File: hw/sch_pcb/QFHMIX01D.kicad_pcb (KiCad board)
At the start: 2 copper layers, 90.9 x 90.9 mm, 205 parts, among them J1 HEADER_1x08, J2 +9V, M1 HOLE, M2 HOLE, M3 HOLE, M4 HOLE, M5 HOLE, M6 HOLE, M7 HOLE, M8 HOLE, U1 NCP1117ST33, U11 TPS563249, U12 Si53322, U2 AD8343, U3 AD8343, U5 LT6604-10, U6 MPGA-105+, U7 MPGA-105+, U8 MGVA-63+, U9 MGVA-63+

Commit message: Zmena pouzdra L 0805
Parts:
- L1, L10, L11, L12, L13, L14, L15, L16, L17, L18, L19, L2, L20, L21, L22, L23, L24, L25, L26, L27, L28, L29, L3, L30, L31, L32, L33, L34, L35, L36, L37, L38, L39, L4, L40, L41, L42, L43, L44, L45, L46, L47, L5, L52, L53, L54, L55, L56, L57, L58, L59, L6, L60, L61, L62, L63, L64, L65, L66, L67, L68, L69, L7, L70, L8, L9: footprint Inductor_SMD:L_0805_2012Metric -> Inductor_SMD:L_0805_2012Metric_Pad1.15x1.40mm_HandSolder
- L48: footprint Mlab_L:SMD-0805 -> Inductor_SMD:L_0805_2012Metric_Pad1.15x1.40mm_HandSolder
- L51: footprint Mlab_R:SMD-0805 -> Inductor_SMD:L_0805_2012Metric_Pad1.15x1.40mm_HandSolder

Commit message: Add thermistor #22, align text labels
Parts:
- added D2: BZV55C-3,6V, Diode_SMD:D_MiniMELF, B.Cu at (171.9, 117.3)
- added R16: 24k, Resistor_SMD:R_0805_2012Metric, B.Cu at (167.5, 117.5)
- added TH1: Thermistor, NCP21XV103J03RA, Resistor_SMD:R_0805_2012Metric, B.Cu at (140.5, 98.4)
- moved R3 1.81 mm to (146.8, 97.2)
- moved R6 0.99 mm to (145.4, 91.3), turned to 45 degrees
- moved C12 0.40 mm to (137.6, 87.7)
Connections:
- U11 pad 5: VCC -> /Power/PWR_EN
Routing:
- net /Power/PWR_EN: track 0.00 -> 55.5 mm, vias 0 -> 6
- net VCC: track 69.9 -> 65.6 mm, vias 5 -> 4
- net +5V: track 186.3 -> 182.1 mm
- net Net-(L3-Pad1): track 1.83 -> 2.49 mm
- net GND: vias 510 -> 511
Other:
- board text added: "mlab.cz 2022"
- board text removed: "mlab.cz 2021"

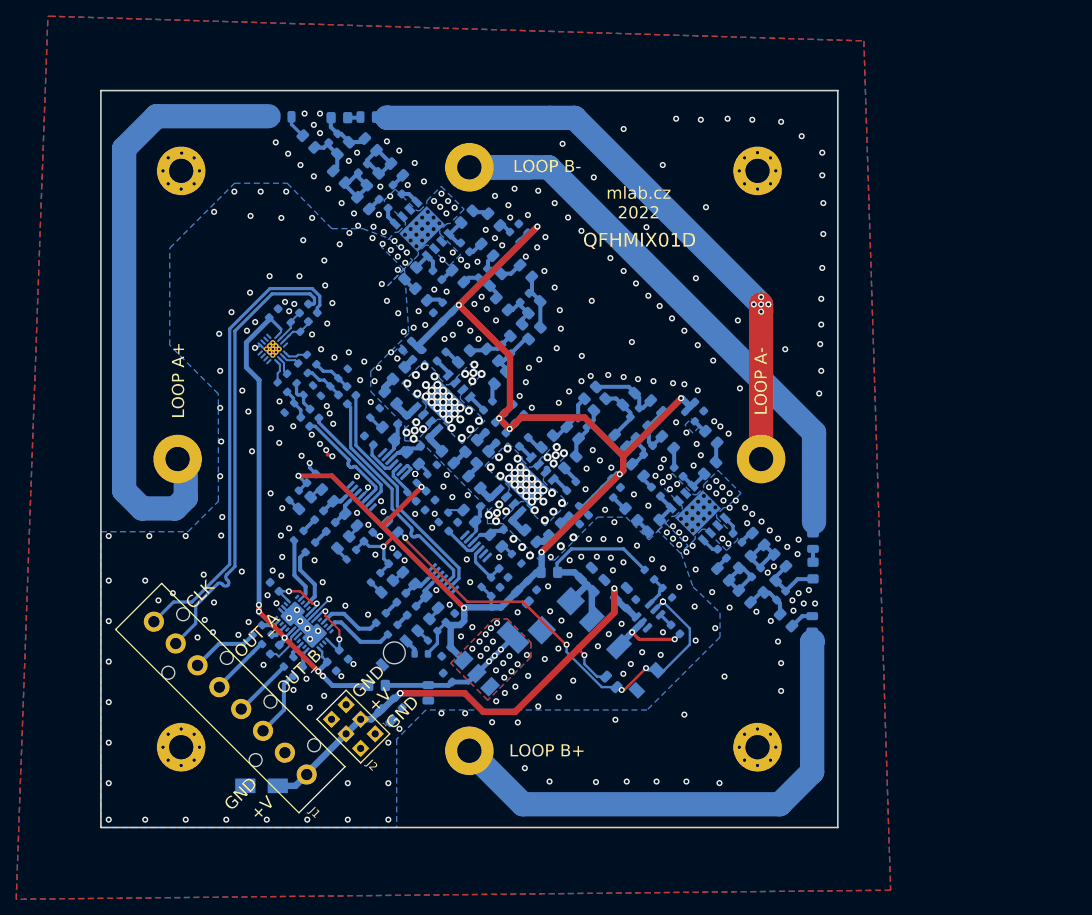
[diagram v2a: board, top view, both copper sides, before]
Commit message: reseni nekterych DRC prolemu
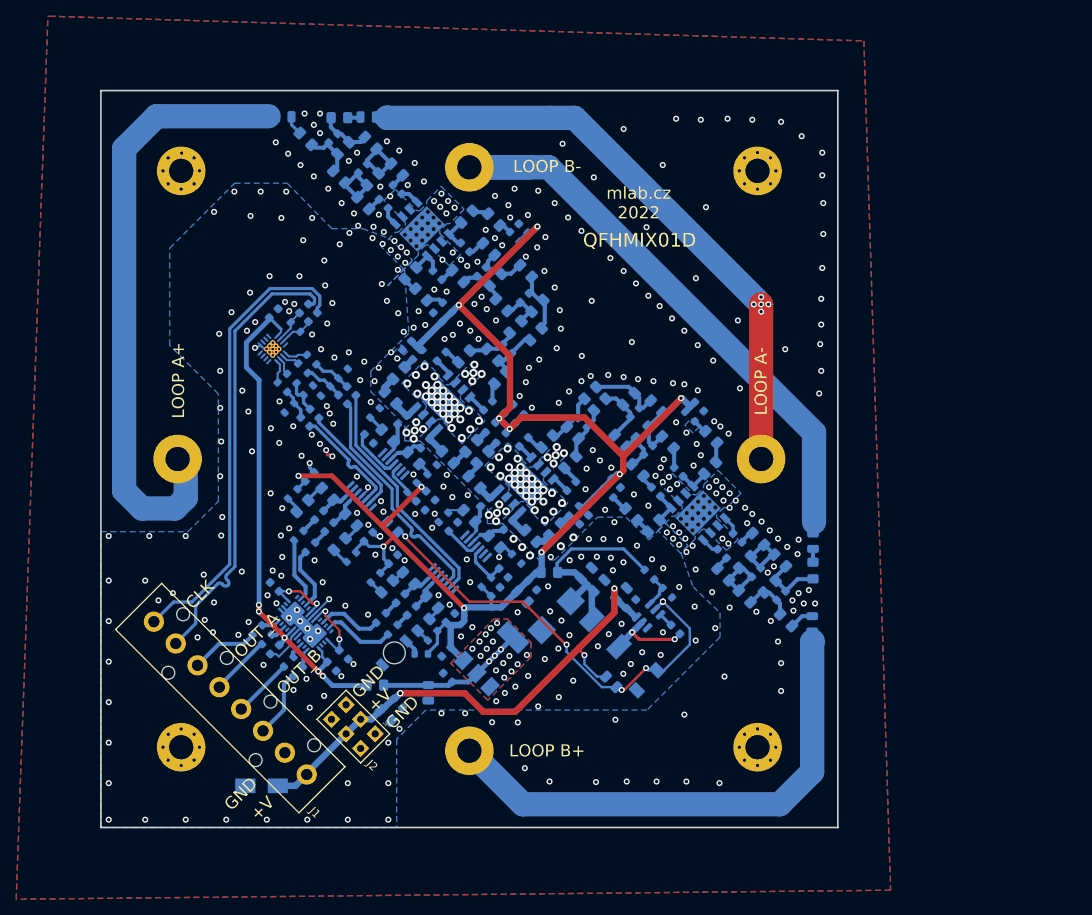
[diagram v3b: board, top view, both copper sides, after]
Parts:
- moved L5 0.50 mm to (129.8, 50.5)
- moved L12 0.49 mm to (134.0, 100.5)
- moved L8 0.47 mm to (129.4, 95.8)
- moved L36 0.42 mm to (158.4, 71.1)
- moved L39 0.40 mm to (155.7, 73.7)
- moved L2 0.31 mm to (139.9, 87.1)
- moved R26 0.30 mm to (135.4, 102.1)
- moved C17 0.27 mm to (130.3, 92.2)
- moved C58 0.26 mm to (151.5, 66.9)
- moved R24 0.25 mm to (128.2, 94.3)
- moved L1 0.22 mm to (153.1, 100.2)
- moved L59 0.22 mm to (152.4, 64.1)
- moved C36 0.22 mm to (144.5, 88.1)
- moved L48 0.21 mm to (138.4, 117.9)
- moved L65 0.21 mm to (158.2, 74.6)
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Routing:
- net GND: track 27.7 -> 24.4 mm, vias 511 -> 510
- net Net-(C12-Pad1): track 4.88 -> 6.51 mm
- net +5V: track 182.1 -> 181.0 mm
- net Net-(C74-Pad2): track 26.4 -> 25.7 mm
- net Net-(C58-Pad2): track 5.60 -> 4.95 mm
- net Net-(C64-Pad2): track 6.83 -> 6.25 mm
- net Net-(C63-Pad2): track 5.27 -> 4.69 mm

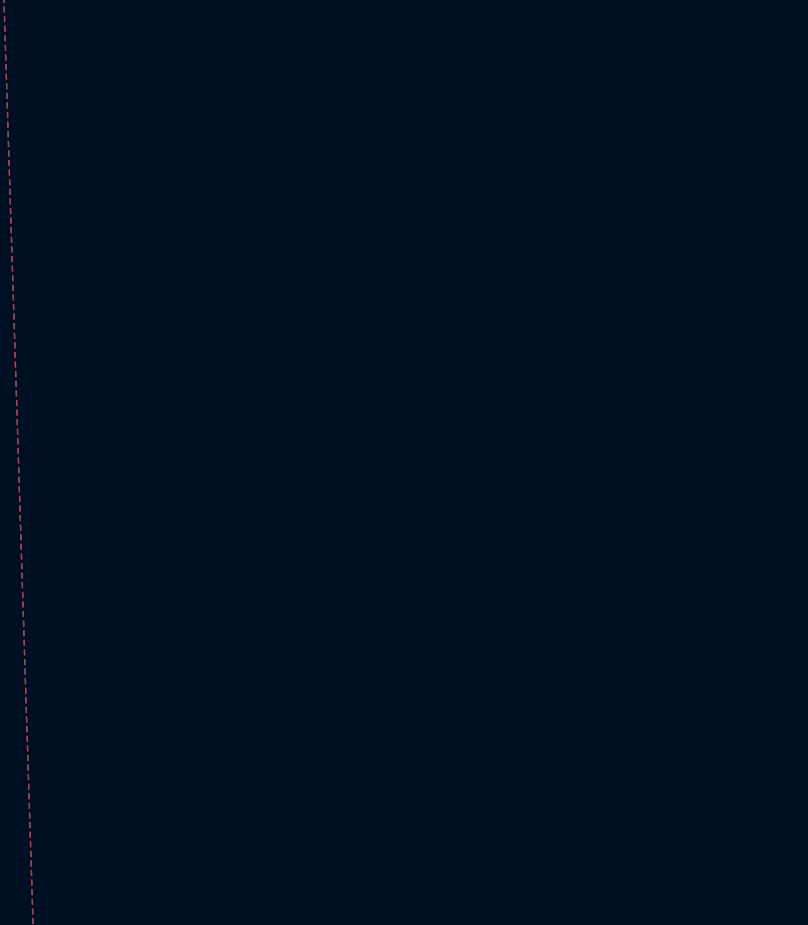
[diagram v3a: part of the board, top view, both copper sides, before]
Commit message: rozpracovani #11 (menic na 5 a 3v3)
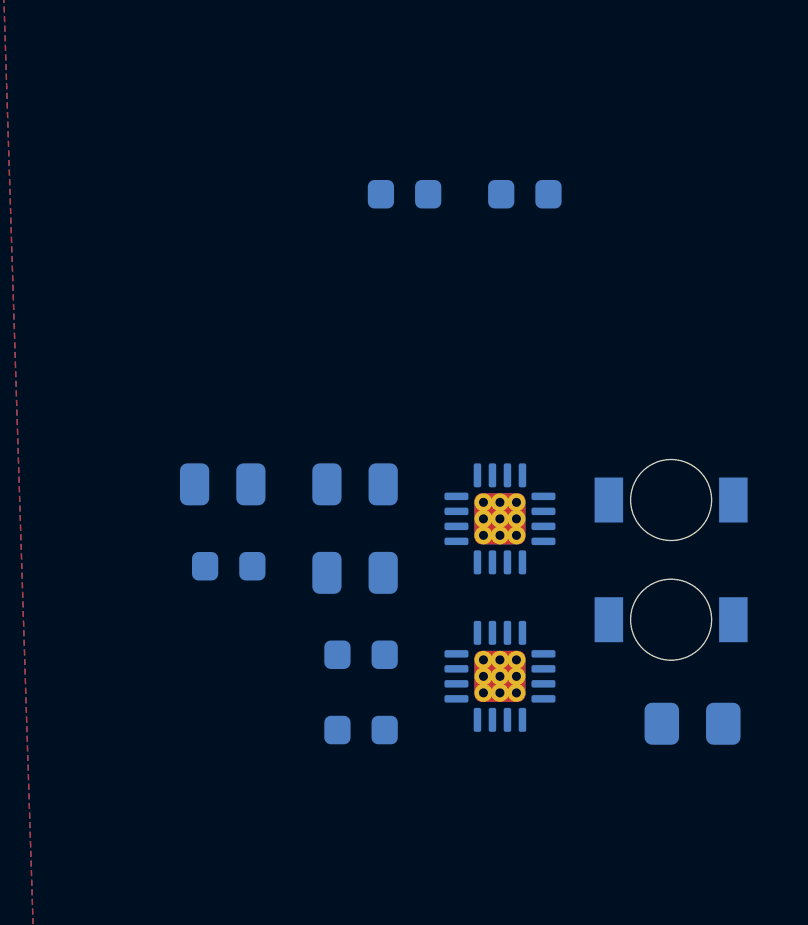
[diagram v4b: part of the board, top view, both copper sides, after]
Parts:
- added C66: 10uF/16, Capacitor_SMD:C_0805_2012Metric, B.Cu at (211.8, 102.1)
- added C67: 100nF, Capacitor_SMD:C_0603_1608Metric, B.Cu at (212.0, 107.3)
- added C68: 10uF/16, Capacitor_SMD:C_0805_2012Metric, B.Cu at (207.4, 99.1)
- added C69: 100nF, Capacitor_SMD:C_0603_1608Metric, B.Cu at (212.0, 104.8)
- added C86: 47uF/6,3V, Capacitor_SMD:C_0805_2012Metric, B.Cu at (211.8, 99.1)
- added C87: 100nF, Capacitor_SMD:C_0603_1608Metric, B.Cu at (207.6, 101.8)
- added D3: RED, Mlab_D:LED_1206, B.Cu at (222.3, 103.6)
- added D4: RED, Mlab_D:LED_1206, B.Cu at (222.3, 99.6)
- added L73: BLM21PG331SN1D, Inductor_SMD:L_0805_2012Metric_Pad1.15x1.40mm_HandSolder, B.Cu at (223.0, 107.1)
- added R41: 180k, Resistor_SMD:R_0603_1608Metric, B.Cu at (217.4, 89.4)
- added R42: 25k, Resistor_SMD:R_0603_1608Metric, B.Cu at (213.4, 89.4)
- added U11: LTC3601, Package_DFN_QFN:QFN-16-1EP_3x3mm_P0.5mm_EP1.7x1.7mm_ThermalVias, B.Cu at (216.6, 105.5)
- added U9: LTC3601, Package_DFN_QFN:QFN-16-1EP_3x3mm_P0.5mm_EP1.7x1.7mm_ThermalVias, B.Cu at (216.6, 100.3)
- renumbered C2 to C1, C4 to C10, C5 to C11, C6 to C12, C7 to C13, C15 to C14, C16 to C15, C17 to C16, C18 to C17, C19 to C18, C20 to C19, C1 to C2, C21 to C20, C22 to C21, C23 to C22, C24 to C23, C25 to C24, C26 to C25, C27 to C26, C28 to C27, C14 to C28, C31 to C29, C34 to C30, C39 to C31, C40 to C33, C45 to C34, C46 to C35, C47 to C36, C33 to C37, C55 to C38, C48 to C39, C8 to C4, C42 to C40, C56 to C42, C57 to C43, C43 to C44, C49 to C45, C50 to C46, C44 to C47, C51 to C48, C58 to C49, C9 to C5, C52 to C50, C63 to C51, C64 to C52, C65 to C53, C53 to C55, C29 to C56, C30 to C57, C59 to C58, C60 to C59, C10 to C6, C61 to C60, C62 to C61, C35 to C62, C36 to C63, C37 to C64, C38 to C65, C11 to C7, C68 to C71, C70 to C73, C72 to C76, C74 to C77, C76 to C78, C78 to C79, C12 to C8, C80 to C82, C82 to C84, C66 to C88, C67 to C89, C13 to C9, C69 to C90, D3 to D5, L11 to L10, L12 to L11, L13 to L12, L5 to L13, L62 to L18, L52 to L19, L53 to L20, L27 to L21, L28 to L22, L54 to L23, L33 to L24, L55 to L25, L56 to L26, L34 to L27, L57 to L28, L20 to L29, L21 to L30, L18 to L31, L19 to L32, L24 to L33, L25 to L34, L22 to L35, L23 to L36, L64 to L37, L26 to L38, L58 to L39, L59 to L40, L29 to L41, L30 to L42, L31 to L43, L32 to L44, L60 to L45, L61 to L46, L35 to L47, L36 to L48, L37 to L49, L6 to L5, L38 to L50, L39 to L51, L65 to L52, L66 to L53, L67 to L54, L68 to L55, L70 to L56, L69 to L57, L63 to L58, L40 to L59, L7 to L6, L41 to L60, L42 to L61, L43 to L62, L44 to L63, L45 to L64, L46 to L65, L47 to L66, L48 to L69, L8 to L7, L49 to L70, L51 to L71, L9 to L8, L10 to L9, M2 to M1, M1 to M2, R12 to R1, R4 to R10, R5 to R11, R9 to R12, R10 to R13, R7 to R14, R8 to R15, R23 to R16, R24 to R17, R25 to R18, R26 to R19, R1 to R2, R27 to R20, R28 to R21, R29 to R22, R30 to R23, R31 to R24, R32 to R25, R33 to R26, R34 to R27, R36 to R28, R35 to R29, R2 to R3, R38 to R30, R37 to R31, R39 to R32, R40 to R33, R41 to R34, R42 to R35, R16 to R36, R48 to R39, R3 to R4, R52 to R40, R54 to R45, R6 to R5, R11 to R6, R13 to R7, R14 to R8, R15 to R9, U12 to U1, U11 to U10, U1 to U12, U5 to U4, U6 to U5, U7 to U6, U8 to U7, U9 to U8
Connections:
- C89 pad 2: /Power/3V3VO -> Net-(C89-Pad2)
- C90 pad 1: /Power/3V3VO -> Net-(C89-Pad2)
- U12 pad 2: /Power/3V3VO -> Net-(C89-Pad2)
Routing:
- net Net-(C89-Pad2): track 0.00 -> 18.3 mm, vias 0 -> 3
- net /Power/3V3VO: track 18.3 -> 0.00 mm, vias 18 -> 15

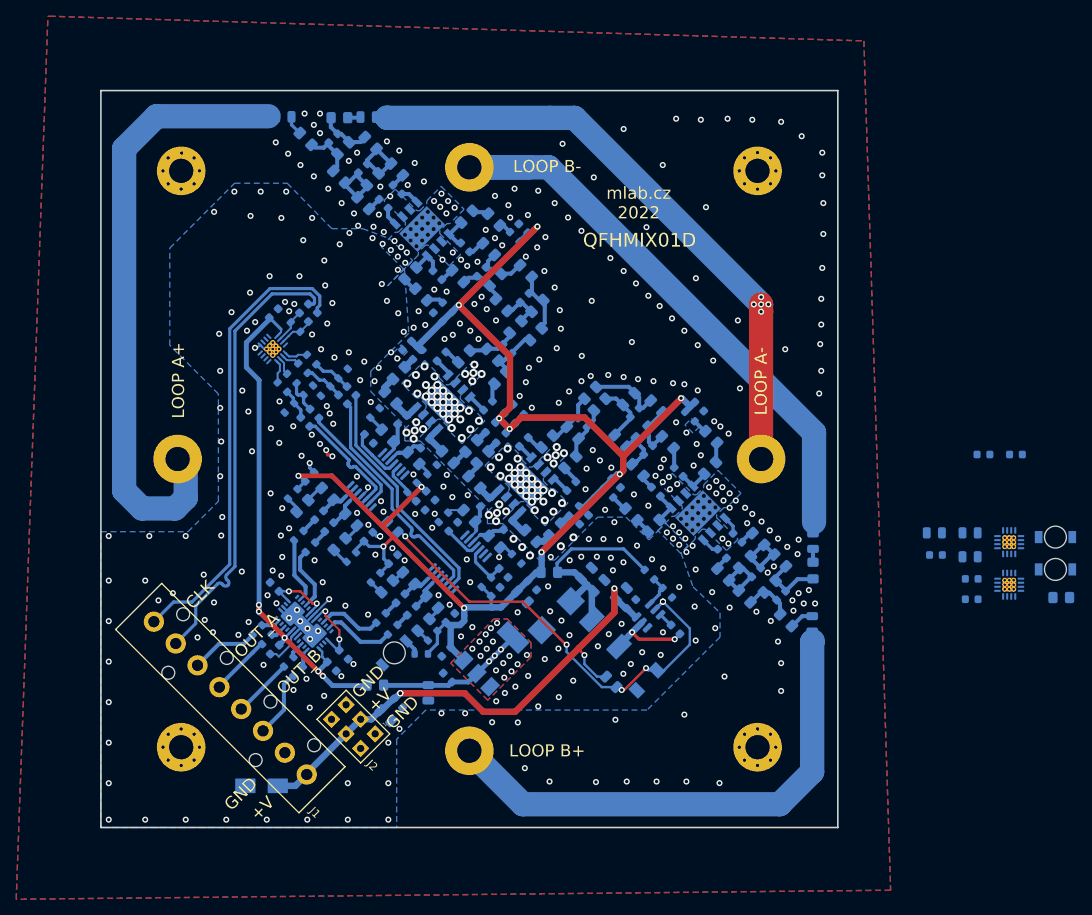
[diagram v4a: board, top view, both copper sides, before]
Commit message: Pridani novych otvoru pro sloupky pro montaz anteny #20, WIP
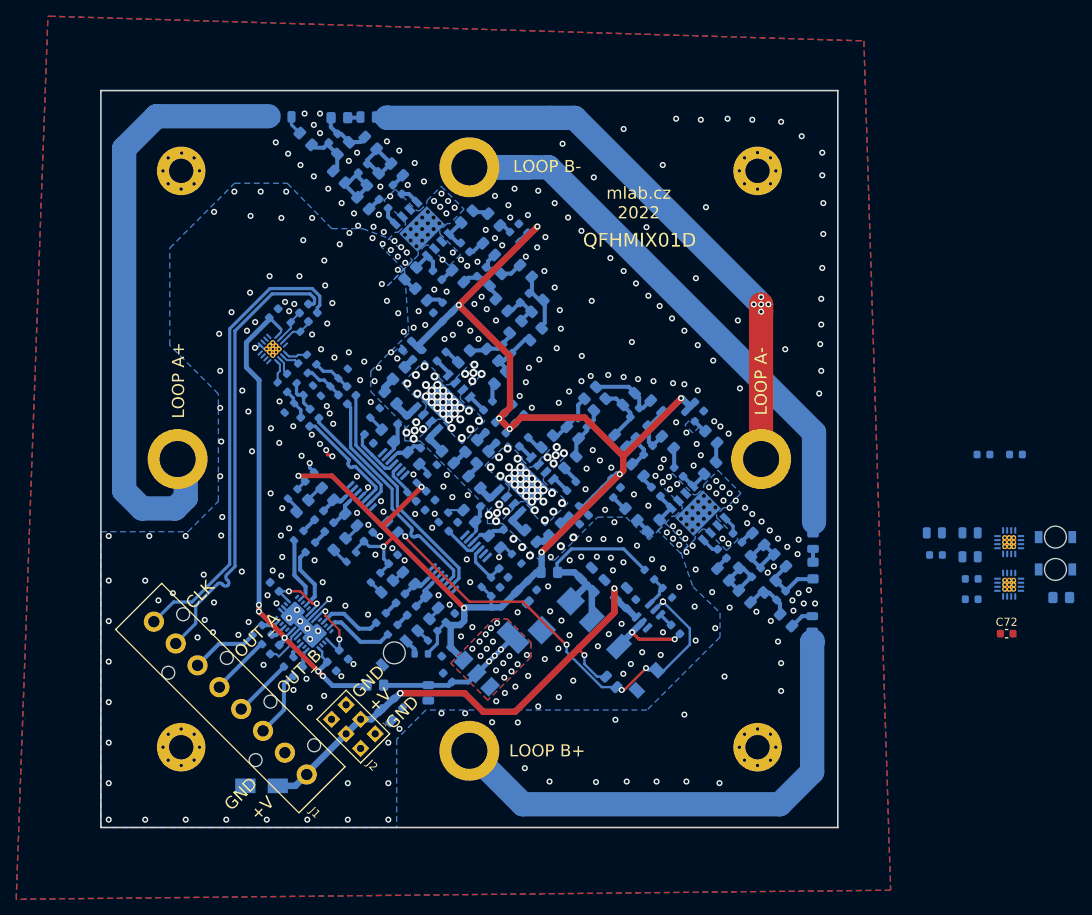
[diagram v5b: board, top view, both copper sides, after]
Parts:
- added C72: 100nF, Capacitor_SMD:C_0603_1608Metric, F.Cu at (216.3, 111.5)
- M1, M2, M3, M4: footprint Mlab_Mechanical:MountingHole_3mm -> Mlab_Mechanical:WA-SMSI_SMT_Steel_Spacer
- renumbered C71 to C68, C73 to C70, C66 to C73, C67 to C74, C76 to C75, C68 to C76, C69 to C77, C77 to C78, C78 to C79, C79 to C80, C82 to C84, C84 to C86, C86 to C87, C87 to C88, C88 to C89, C89 to C90, C90 to C91, L71 to L72, R39 to R42, R40 to R43, R41 to R44, R42 to R45, R45 to R47
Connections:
- L69 pad 1: /Power/3V3VO -> unconnected-(L69-Pad1)
- L69 pad 2: +3V3 -> unconnected-(L69-Pad2)
- L73 pad 1: /Power/5VO -> unconnected-(L73-Pad1)
- L73 pad 2: +5V -> unconnected-(L73-Pad2)
- R44 pad 1: /Power/5VO -> +5V
- U11 pad 1: Net-(C81-Pad1) (its old number) -> GND
- U11 pad 10: Net-(C81-Pad1) (its old number) -> Net-(R46-Pad1)
- U11 pad 12: Net-(C81-Pad1) (its old number) -> Net-(C82-Pad1)
- U11 pad 7: Net-(C81-Pad1) (its old number) -> Net-(C82-Pad1)
- U11 pad 8: /Power/5VO -> +5V
- U9 pad 1: Net-(C72-Pad1) -> GND
- U9 pad 10: Net-(C72-Pad1) -> Net-(R39-Pad1)
- U9 pad 12: Net-(C72-Pad1) -> Net-(C67-Pad1)
- U9 pad 7: Net-(C72-Pad1) -> Net-(C67-Pad1)
- U9 pad 8: /Power/3V3VO -> +3V3
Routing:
- net /Power/3V3VO: vias 15 -> 0
- net +3V3: vias 5 -> 20
- added copper zone on B.Cu, net +3V3
- added copper zone on F.Cu, net +3V3
- removed copper zone on B.Cu, net /Power/3V3VO
- removed copper zone on F.Cu, net /Power/3V3VO
